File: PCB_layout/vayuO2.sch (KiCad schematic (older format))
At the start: 60 parts, among them CN1 Conn_LED, CN14 Conn_Analog, CN15 Conn_ADS1115, CN16 Conn_S1, CN17 Conn_S2, CN18 Conn_S3, CN2 UART1, CN3 UART2, CN4 qwiic, CN5 qwiic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

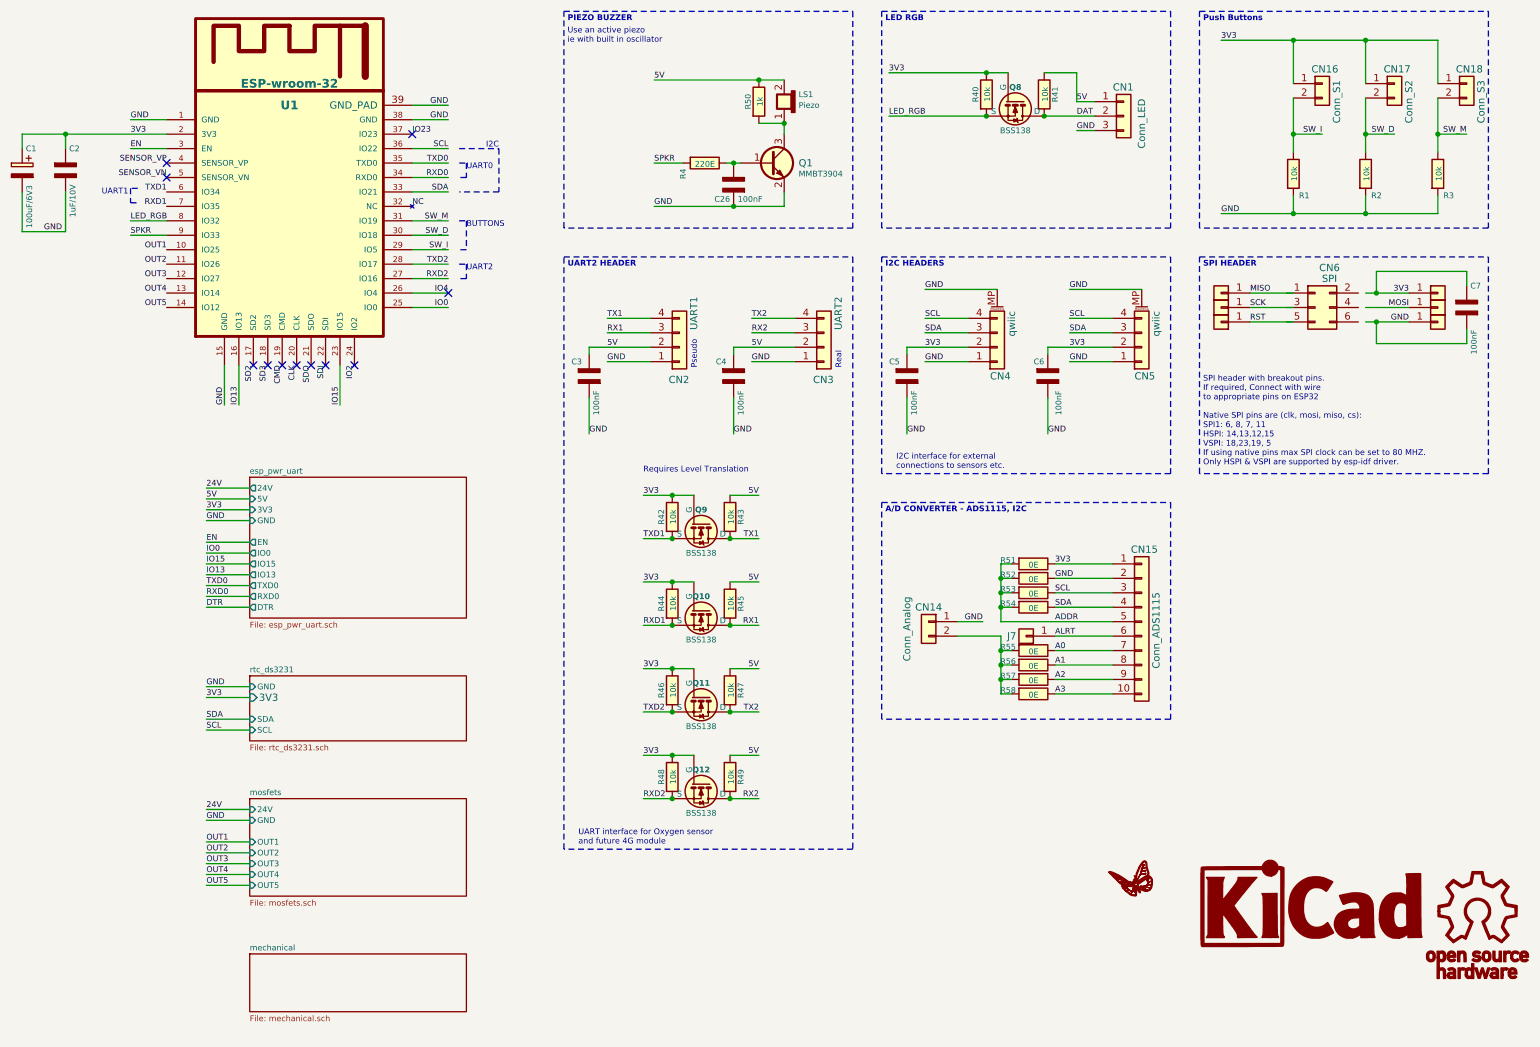
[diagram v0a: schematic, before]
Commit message: added optocoupler for isolation
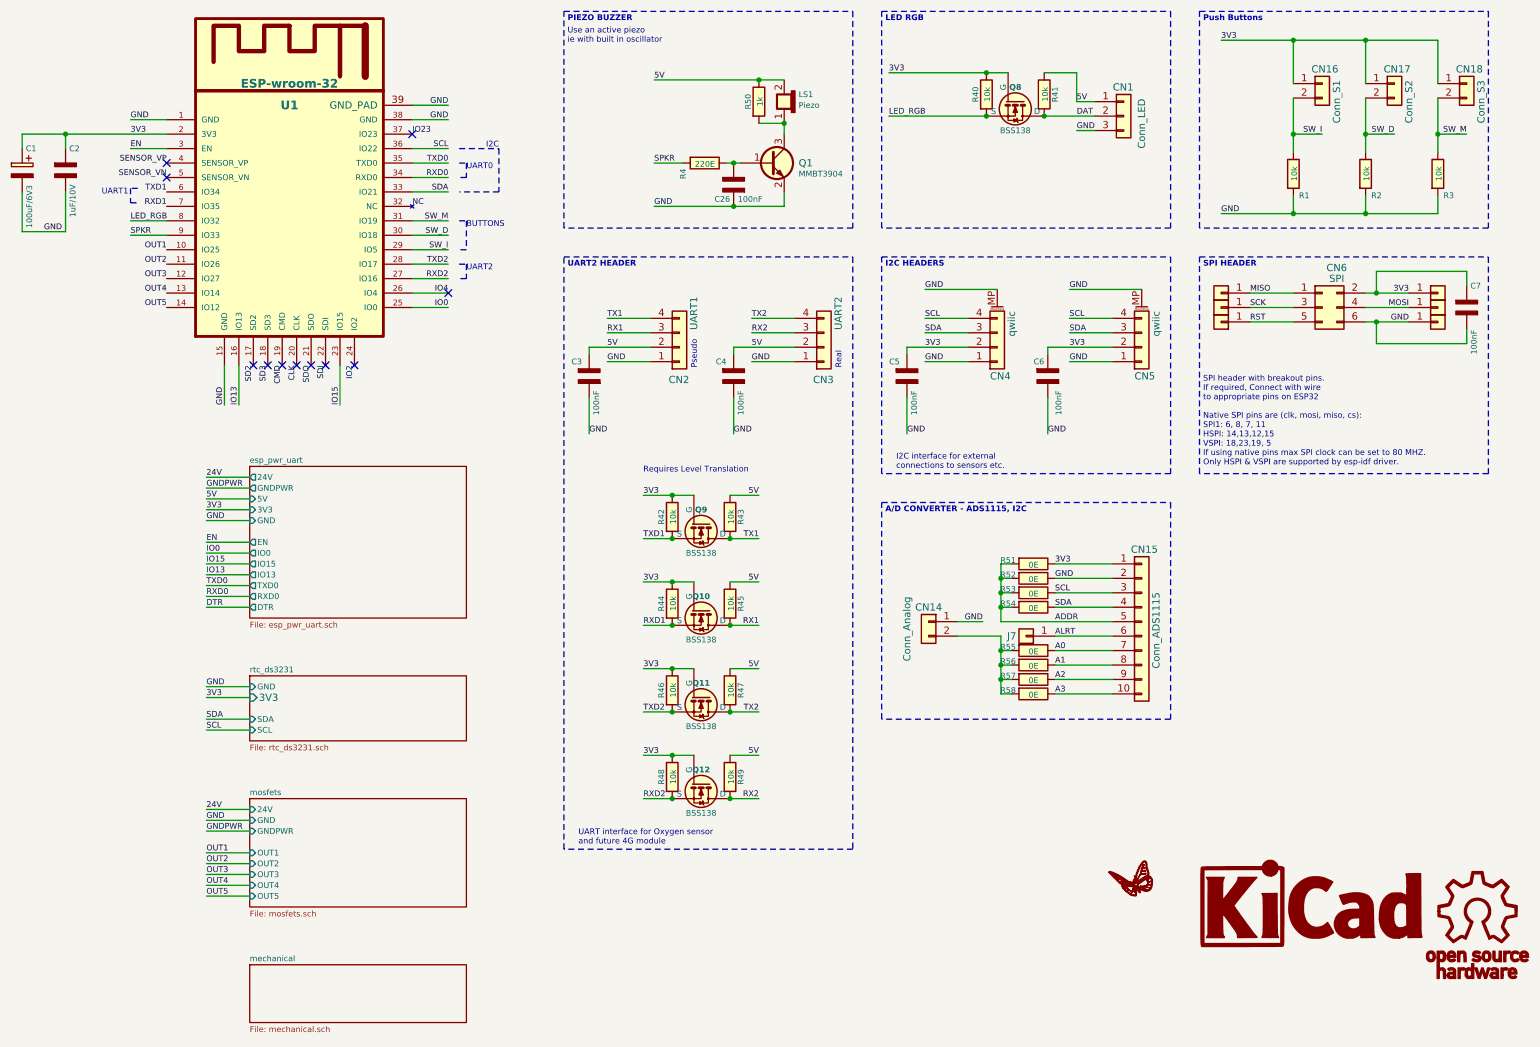
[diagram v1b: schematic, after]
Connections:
- net labels added: GNDPWR
- wire segments 176 -> 178
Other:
- moved on the sheet: CN6
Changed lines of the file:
@@
 $EndComp
 $Sheet
-S 2350 7200 1500 400
+S 2350 7275 1500 400
 U 5A47432D
 F0 "mechanical" 40
@@
 SCL
 $Sheet
-S 2350 3900 1500 975
+S 2350 3825 1500 1050
 U 5A452227
 F0 "esp_pwr_uart" 40
@@
 F10 "RXD0" O L 2350 4725 40
 F11 "DTR" O L 2350 4800 40
-F12 "24V" O L 2350 3975 40
+F12 "24V" O L 2350 3900 40
+F13 "GNDPWR" O L 2350 3975 40
 $EndSheet
 Wire Wire Line
@@
 L AA_vayuO2_symbols:Conn_02x03_Odd_Even CN6
 U 1 1 5A590BB3
-P 9775 2725
-F 0 "CN6" H 9825 3000 50  0000 C CNN
-F 1 "SPI" H 9825 2925 50  0000 C CNN
-F 2 "AA_vayu:Header_ISP" H 9775 2725 50  0001 C CNN
-F 3 "~" H 9775 2725 50  0001 C CNN
-	1    9775 2725
+P 9825 2725
+F 0 "CN6" H 9875 3000 50  0000 C CNN
+F 1 "SPI" H 9875 2925 50  0000 C CNN
+F 2 "AA_vayu:Header_ISP" H 9825 2725 50  0001 C CNN
+F 3 "~" H 9825 2725 50  0001 C CNN
+	1    9825 2725
 	1    0    0    -1
 $EndComp
@@
 Requires Level Translation
 $Sheet
-S 2350 6125 1500 675
+S 2350 6125 1500 750
 U 6178DB6E
 F0 "mosfets" 40
@@
 F2 "24V" I L 2350 6200 40
 F3 "GND" I L 2350 6275 40
-F4 "OUT1" I L 2350 6425 40
-F5 "OUT2" I L 2350 6500 40
-F6 "OUT3" I L 2350 6575 40
-F7 "OUT4" I L 2350 6650 40
-F8 "OUT5" I L 2350 6725 40
+F4 "OUT1" I L 2350 6500 40
+F5 "OUT2" I L 2350 6575 40
+F6 "OUT3" I L 2350 6650 40
+F7 "OUT4" I L 2350 6725 40
+F8 "OUT5" I L 2350 6800 40
+F9 "GNDPWR" I L 2350 6350 40
 $EndSheet
 Text Notes 1325 1950 0    40   ~ 0
@@
 GND
 Wire Wire Line
-	2050 3975 2350 3975
-Text Label 2050 3975 0    40   ~ 0
+	2050 3900 2350 3900
+Text Label 2050 3900 0    40   ~ 0
 24V
 Wire Wire Line
 	2050 6200 2350 6200
 Wire Wire Line
-	2050 6425 2350 6425
-Wire Wire Line
 	2050 6500 2350 6500
 Wire Wire Line
@@
 Wire Wire Line
 	2050 6725 2350 6725
+Wire Wire Line
+	2050 6800 2350 6800
 Text Label 2050 6200 0    40   ~ 0
 24V
+Text Label 2050 6650 0    40   ~ 0
+OUT3
+Text Label 2050 6725 0    40   ~ 0
+OUT4
+Text Label 2050 6800 0    40   ~ 0
+OUT5
+Text Label 2050 6500 0    40   ~ 0
+OUT1
 Text Label 2050 6575 0    40   ~ 0
-OUT3
-Text Label 2050 6650 0    40   ~ 0
-OUT4
-Text Label 2050 6725 0    40   ~ 0
-OUT5
-Text Label 2050 6425 0    40   ~ 0
-OUT1
-Text Label 2050 6500 0    40   ~ 0
 OUT2
 $Comp
@@
 	1    0    0    -1
 $EndComp
+Wire Wire Line
+	2350 3975 2050 3975
+Text Label 2050 3975 0    40   ~ 0
+GNDPWR
+Wire Wire Line
+	2050 6350 2350 6350
+Text Label 2050 6350 0    40   ~ 0
+GNDPWR
 $EndSCHEMATC

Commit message: PCB layout, WIP
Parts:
- removed C7: 100nF, AA_vayu:C_0603_1608Metric, symbol AA_vayuO2_symbols:C_NP
- removed CN6: SPI, AA_vayu:Header_ISP, symbol AA_vayuO2_symbols:Conn_02x03_Odd_Even
- removed J1: MISO, AA_vayu:BreakOutPad, symbol AA_vayuO2_symbols:Conn_01x01
- removed J2: 3V3, AA_vayu:BreakOutPad, symbol AA_vayuO2_symbols:Conn_01x01
- removed J3: SCK, AA_vayu:BreakOutPad, symbol AA_vayuO2_symbols:Conn_01x01
- removed J4: MOSI, AA_vayu:BreakOutPad, symbol AA_vayuO2_symbols:Conn_01x01
- removed J5: RST, AA_vayu:BreakOutPad, symbol AA_vayuO2_symbols:Conn_01x01
- removed J6: GND, AA_vayu:BreakOutPad, symbol AA_vayuO2_symbols:Conn_01x01
- CN4: value qwiic -> I2C_1; symbol AA_vayuO2_symbols:Conn_01x04_MountingPin -> AA_vayuO2_symbols:Conn_01x04
- CN5: value qwiic -> I2C_2; symbol AA_vayuO2_symbols:Conn_01x04_MountingPin -> AA_vayuO2_symbols:Conn_01x04
- R51, R52, R53, R54, R55, R56, R57, R58: footprint AA_vayu:R_0603_1608Metric -> AA_vayu:SolderJumper-2_P1.3mm_Open_RoundedPad1.0x1.5mm
- U1: value ESP-wroom-32 -> ESP32-WROOM-32UC; footprint AA_vayu:ESP_wroom_32 -> AA_vayu:ESP_wroom_32_ext_ant
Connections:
- net GND: no longer CN4.MP (MountPin), CN5.MP (MountPin)
- net OUT1: now also U1.14 (IO12); no longer U1.10 (IO25)
- net OUT2: now also U1.13 (IO14); no longer U1.11 (IO26)
- net OUT4: now also U1.11 (IO26); no longer U1.13 (IO14)
- net OUT5: now also U1.10 (IO25); no longer U1.14 (IO12)
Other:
- note added: "NOTE : REMOVED since not required\n\nSPI header with breakout pins.\nIf required, Connect with wire \nto appropriate pins on ESP32"
- note added: "UART HEADERS"
- note removed: "SPI header with breakout pins.\nIf required, Connect with wire \nto appropriate pins on ESP32"
- note removed: "UART2 HEADER"
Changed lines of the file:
@@
 P 2625 2925
 F 0 "U1" H 2625 4525 60  0000 C CNB
-F 1 "ESP-wroom-32" H 2625 4675 60  0000 C CNB
-F 2 "AA_vayu:ESP_wroom_32" H 2625 2925 60  0001 C CNN
+F 1 "ESP32-WROOM-32UC" H 2625 4675 60  0000 C CNB
+F 2 "AA_vayu:ESP_wroom_32_ext_ant" H 2625 2925 60  0001 C CNN
 F 3 "" H 2625 2925 60  0001 C CNN
 F 4 "mfr_pn" H 2625 2925 60  0001 C CNN "manf#"
@@
 F0 "mechanical" 40
 F1 "mechanical.sch" 40
+F2 "5V" I L 2350 7425 40
+F3 "GND" I L 2350 7525 40
 $EndSheet
 $Sheet
@@
 Native SPI pins are (clk, mosi, miso, cs):\nSPI1: 6, 8, 7, 11\nHSPI: 14,13,12,15\nVSPI: 18,23,19, 5\nIf using native pins max SPI clock can be set to 80 MHZ.\nOnly HSPI & VSPI are supported by esp-idf driver.
 $Comp
-L AA_vayuO2_symbols:Conn_02x03_Odd_Even CN6
+L AA_vayuO2_symbols:Conn_02x03_Odd_Even #CN6
 U 1 1 5A590BB3
 P 9825 2725
-F 0 "CN6" H 9875 3000 50  0000 C CNN
+F 0 "#CN6" H 9875 3000 50  0000 C CNN
 F 1 "SPI" H 9875 2925 50  0000 C CNN
 F 2 "AA_vayu:Header_ISP" H 9825 2725 50  0001 C CNN
@@
 Text Label 9275 2825 0    40   ~ 0
 RST
-Text Label 1775 2625 2    40   ~ 0
+Text Label 1775 2425 2    40   ~ 0
 OUT4
-Text Label 1775 2725 2    40   ~ 0
+Text Label 1775 2325 2    40   ~ 0
 OUT5
 $Comp
-L AA_vayuO2_symbols:Conn_01x01 J1
+L AA_vayuO2_symbols:Conn_01x01 #J1
 U 1 1 5A6285C8
 P 9075 2625
-F 0 "J1" H 8975 2475 50  0001 C CNN
+F 0 "#J1" H 8975 2475 50  0001 C CNN
 F 1 "MISO" H 8975 2475 50  0001 C CNN
 F 2 "AA_vayu:BreakOutPad" H 9075 2625 50  0001 C CNN
@@
 $EndComp
 $Comp
-L AA_vayuO2_symbols:Conn_01x01 J3
+L AA_vayuO2_symbols:Conn_01x01 #J3
 U 1 1 5A63BBF7
 P 9075 2725
-F 0 "J3" H 8975 2575 50  0001 C CNN
+F 0 "#J3" H 8975 2575 50  0001 C CNN
 F 1 "SCK" H 8975 2575 50  0001 C CNN
 F 2 "AA_vayu:BreakOutPad" H 9075 2725 50  0001 C CNN
@@
 $EndComp
 $Comp
-L AA_vayuO2_symbols:Conn_01x01 J5
+L AA_vayuO2_symbols:Conn_01x01 #J5
 U 1 1 5A63BDD4
 P 9075 2825
-F 0 "J5" H 8975 2675 50  0001 C CNN
+F 0 "#J5" H 8975 2675 50  0001 C CNN
 F 1 "RST" H 8975 2675 50  0001 C CNN
 F 2 "AA_vayu:BreakOutPad" H 9075 2825 50  0001 C CNN
@@
 $EndComp
 $Comp
-L AA_vayuO2_symbols:Conn_01x01 J6
+L AA_vayuO2_symbols:Conn_01x01 #J6
 U 1 1 5A63C3B0
 P 10575 2825
-F 0 "J6" H 10475 2675 50  0001 C CNN
+F 0 "#J6" H 10475 2675 50  0001 C CNN
 F 1 "GND" H 10475 2675 50  0001 C CNN
 F 2 "AA_vayu:BreakOutPad" H 10575 2825 50  0001 C CNN
@@
 $EndComp
 $Comp
-L AA_vayuO2_symbols:Conn_01x01 J4
+L AA_vayuO2_symbols:Conn_01x01 #J4
 U 1 1 5A63C933
 P 10575 2725
-F 0 "J4" H 10475 2575 50  0001 C CNN
+F 0 "#J4" H 10475 2575 50  0001 C CNN
 F 1 "MOSI" H 10475 2575 50  0001 C CNN
 F 2 "AA_vayu:BreakOutPad" H 10575 2725 50  0001 C CNN
@@
 $EndComp
 $Comp
-L AA_vayuO2_symbols:Conn_01x01 J2
+L AA_vayuO2_symbols:Conn_01x01 #J2
 U 1 1 5A63CDCD
 P 10575 2625
-F 0 "J2" H 10475 2475 50  0001 C CNN
+F 0 "#J2" H 10475 2475 50  0001 C CNN
 F 1 "3V3" H 10475 2475 50  0001 C CNN
 F 2 "AA_vayu:BreakOutPad" H 10575 2625 50  0001 C CNN
@@
 $EndComp
 Text Notes 8950 3375 0    40   ~ 0
-SPI header with breakout pins.\nIf required, Connect with wire \nto appropriate pins on ESP32
+NOTE : REMOVED since not required\n\nSPI header with breakout pins.\nIf required, Connect with wire \nto appropriate pins on ESP32
 Wire Notes Line
 	8925 675  10925 675
@@
 GND
 $Comp
-L AA_vayuO2_symbols:Conn_01x04_MountingPin CN5
+L AA_vayuO2_symbols:Conn_01x04 CN5
 U 1 1 5A7E9B9A
 P 8525 3000
 F 0 "CN5" H 8475 3200 50  0000 L CNN
-F 1 "qwiic" V 8625 2750 50  0000 L CNN
+F 1 "I2C_2" V 8625 2750 50  0000 L CNN
 F 2 "AA_vayu:JST_EH_B4B-EH-A_1x04_P2.50mm_Vertical" H 8525 3000 50  0001 C CNN
 F 3 "~" H 8525 3000 50  0001 C CNN
@@
 I2C HEADERS
 $Comp
-L AA_vayuO2_symbols:C_NP C7
+L AA_vayuO2_symbols:C_NP #C7
 U 1 1 5A8D713D
 P 10775 2725
-F 0 "C7" H 10800 2875 40  0000 L CNN
+F 0 "#C7" H 10800 2875 40  0000 L CNN
 F 1 "100nF" V 10825 2400 40  0000 L CNN
 F 2 "AA_vayu:C_0603_1608Metric" H 10775 2725 60  0001 C CNN
@@
 Text Label 9075 875  0    40   ~ 0
 3V3
-Text Label 1775 2325 2    40   ~ 0
+Text Label 1775 2725 2    40   ~ 0
 OUT1
-Text Label 1775 2425 2    40   ~ 0
+Text Label 1775 2625 2    40   ~ 0
 OUT2
 Wire Wire Line
@@
 	7325 2800 7025 2800
 $Comp
-L AA_vayuO2_symbols:Conn_01x04_MountingPin CN4
+L AA_vayuO2_symbols:Conn_01x04 CN4
 U 1 1 5A79A9A1
 P 7525 3000
 F 0 "CN4" H 7475 3200 50  0000 L CNN
-F 1 "qwiic" V 7625 2750 50  0000 L CNN
+F 1 "I2C_1" V 7625 2750 50  0000 L CNN
 F 2 "AA_vayu:JST_EH_B4B-EH-A_1x04_P2.50mm_Vertical" H 7525 3000 50  0001 C CNN
 F 3 "~" H 7525 3000 50  0001 C CNN
@@
 	4525 6475 4525 2375
 Text Notes 4550 2450 0    40   ~ 8
-UART2 HEADER
+UART HEADERS
 $Comp
 L AA_vayuO2_symbols:C_NP C3
@@
 Wire Wire Line
 	7025 3100 7325 3100
-Text Label 7025 2600 0    40   ~ 0
-GND
-Wire Wire Line
-	7025 2600 7525 2600
-Text Label 8025 2600 0    40   ~ 0
-GND
-Wire Wire Line
-	8025 2600 8525 2600
 Wire Wire Line
 	4825 3100 5125 3100
@@
 F 0 "R51" V 7750 4325 40  0000 C CNN
 F 1 "0E" V 7782 4501 40  0000 C CNN
-F 2 "AA_vayu:R_0603_1608Metric" V 7705 4500 30  0001 C CNN
+F 2 "AA_vayu:SolderJumper-2_P1.3mm_Open_RoundedPad1.0x1.5mm" V 7705 4500 30  0001 C CNN
 F 3 "" H 7775 4500 30  0000 C CNN
 	1    7775 4500
@@
 F 0 "R52" V 7750 4425 40  0000 C CNN
 F 1 "0E" V 7782 4601 40  0000 C CNN
-F 2 "AA_vayu:R_0603_1608Metric" V 7705 4600 30  0001 C CNN
+F 2 "AA_vayu:SolderJumper-2_P1.3mm_Open_RoundedPad1.0x1.5mm" V 7705 4600 30  0001 C CNN
 F 3 "" H 7775 4600 30  0000 C CNN
 	1    7775 4600
@@
 F 0 "R53" V 7750 4525 40  0000 C CNN
 F 1 "0E" V 7782 4701 40  0000 C CNN
-F 2 "AA_vayu:R_0603_1608Metric" V 7705 4700 30  0001 C CNN
+F 2 "AA_vayu:SolderJumper-2_P1.3mm_Open_RoundedPad1.0x1.5mm" V 7705 4700 30  0001 C CNN
 F 3 "" H 7775 4700 30  0000 C CNN
 	1    7775 4700
@@
 F 0 "R54" V 7750 4625 40  0000 C CNN
 F 1 "0E" V 7782 4801 40  0000 C CNN
-F 2 "AA_vayu:R_0603_1608Metric" V 7705 4800 30  0001 C CNN
+F 2 "AA_vayu:SolderJumper-2_P1.3mm_Open_RoundedPad1.0x1.5mm" V 7705 4800 30  0001 C CNN
 F 3 "" H 7775 4800 30  0000 C CNN
 	1    7775 4800
@@
 F 0 "R55" V 7750 4925 40  0000 C CNN
 F 1 "0E" V 7782 5101 40  0000 C CNN
-F 2 "AA_vayu:R_0603_1608Metric" V 7705 5100 30  0001 C CNN
+F 2 "AA_vayu:SolderJumper-2_P1.3mm_Open_RoundedPad1.0x1.5mm" V 7705 5100 30  0001 C CNN
 F 3 "" H 7775 5100 30  0000 C CNN
 	1    7775 5100
@@
 F 0 "R56" V 7750 5025 40  0000 C CNN
 F 1 "0E" V 7782 5201 40  0000 C CNN
-F 2 "AA_vayu:R_0603_1608Metric" V 7705 5200 30  0001 C CNN
+F 2 "AA_vayu:SolderJumper-2_P1.3mm_Open_RoundedPad1.0x1.5mm" V 7705 5200 30  0001 C CNN
 F 3 "" H 7775 5200 30  0000 C CNN
 	1    7775 5200
@@
 F 0 "R57" V 7750 5125 40  0000 C CNN
 F 1 "0E" V 7782 5301 40  0000 C CNN
-F 2 "AA_vayu:R_0603_1608Metric" V 7705 5300 30  0001 C CNN
+F 2 "AA_vayu:SolderJumper-2_P1.3mm_Open_RoundedPad1.0x1.5mm" V 7705 5300 30  0001 C CNN
 F 3 "" H 7775 5300 30  0000 C CNN
 	1    7775 5300
@@
 F 0 "R58" V 7750 5225 40  0000 C CNN
 F 1 "0E" V 7782 5401 40  0000 C CNN
-F 2 "AA_vayu:R_0603_1608Metric" V 7705 5400 30  0001 C CNN
+F 2 "AA_vayu:SolderJumper-2_P1.3mm_Open_RoundedPad1.0x1.5mm" V 7705 5400 30  0001 C CNN
 F 3 "" H 7775 5400 30  0000 C CNN
 	1    7775 5400
@@
 Text Label 2050 6350 0    40   ~ 0
 GNDPWR
+Wire Wire Line
+	2350 7425 2050 7425
+Wire Wire Line
+	2050 7525 2350 7525
+Text Label 2050 7525 0    40   ~ 0
+GND
+Text Label 2050 7425 0    40   ~ 0
+5V
 $EndSCHEMATC

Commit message: BOM, WIP
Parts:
- C1: footprint AA_vayu:CP_Elec_10x10 -> AA_vayu:CP_Elec_8x10
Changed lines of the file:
@@
 F 0 "C1" H 800 1925 40  0000 L CNN
 F 1 "100uF/6V3" V 825 1375 40  0000 L CNN
-F 2 "AA_vayu:CP_Elec_10x10" H 775 1775 60  0001 C CNN
+F 2 "AA_vayu:CP_Elec_8x10" H 775 1775 60  0001 C CNN
 F 3 "" H 775 1775 60  0000 C CNN
 	1    775  1775
